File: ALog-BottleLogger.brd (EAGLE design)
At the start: 120.7 x 44.5 mm, 105 parts, among them IC2 ATMEGA644M, J6 5.5x2.1mm Barrel, Q10 MOSFET_PCH-IRLML2244, Q11 220mA/50V/3.5Ω, Q12 4.3A/20V/54mΩ, Q13 MOSFET-NCH-BSS138, Q5 4.3A/20V/54mΩ, Q7 4.3A/20V/54mΩ, Q8 220mA/50V/3.5Ω, Q9 220mA/50V/3.5Ω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

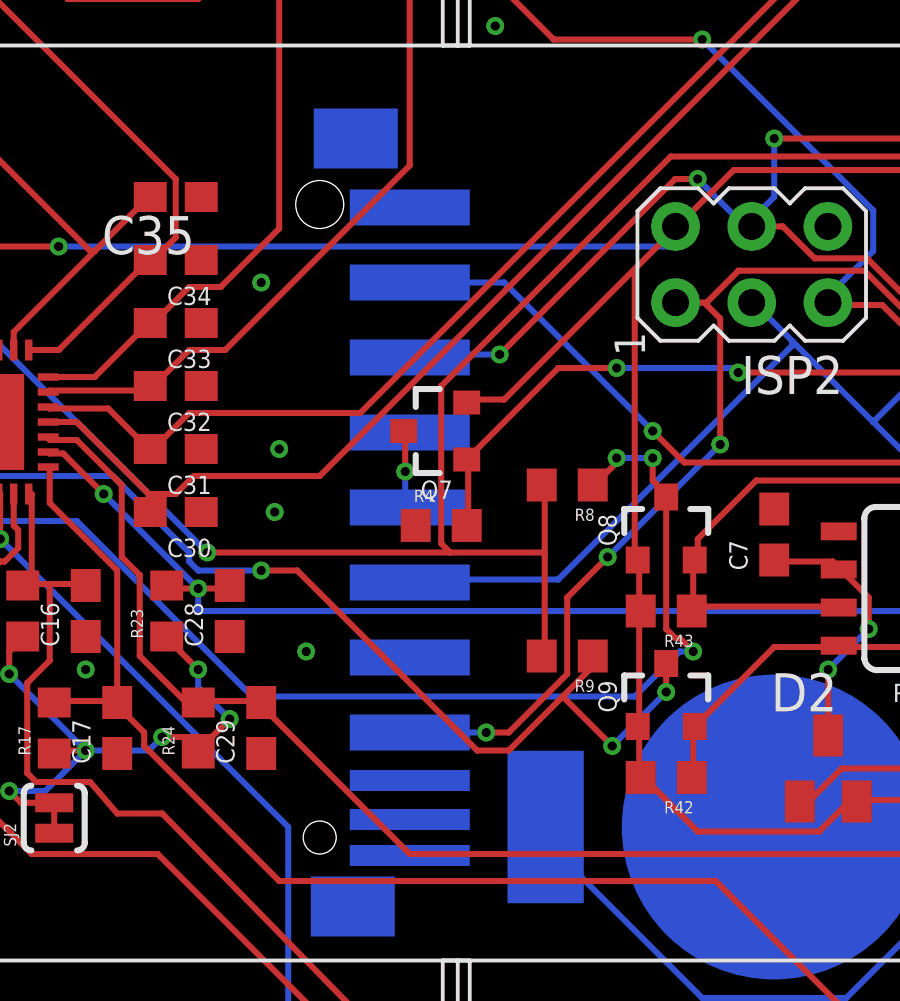
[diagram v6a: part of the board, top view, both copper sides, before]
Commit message: Minor trace fixes, back silkscreen info additions
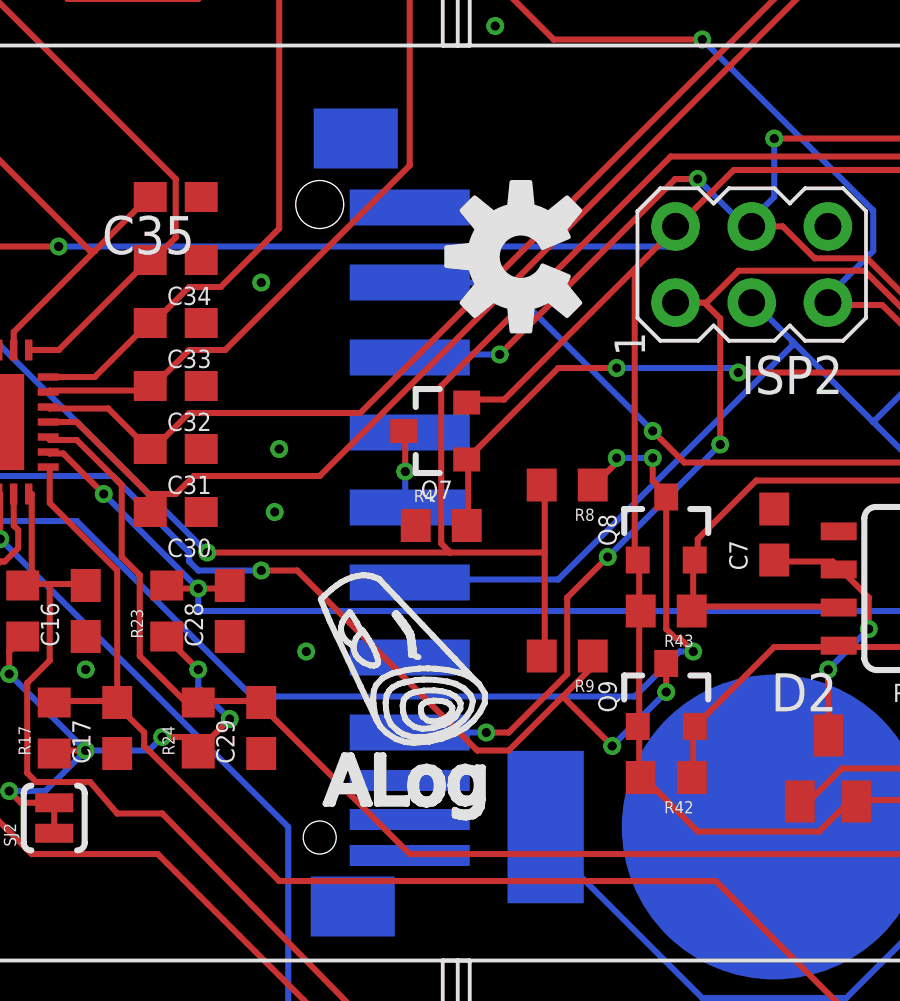
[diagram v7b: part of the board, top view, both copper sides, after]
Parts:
- added LOGO2: OSHW-LOGOM, SparkFun-Aesthetics:OSHW-LOGO-M
- added U$13: (no value), csandell:MN_SILK
- added U$14: ALOG_LOGO_V1_5.5MM, awickert:ALOG_LOGO_V1_SMALL
- added U$15: NWLOGO_MED, awickert:NWLOGO_MED
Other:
- board text added: "ALog BottleLogger v3.0.0 ---------------------------------- Open-source scientific data logger ---------------------------------- Made in Minnesota"
- board text added: "Developed in part at the University of Minnesota in parntnership with Northern Widget LLC"
- board text added: "Open-source for the outdoors"
- board text added: "TM"
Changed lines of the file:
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@@
 <?xml version="1.0" encoding="utf-8"?>
 <!DOCTYPE eagle SYSTEM "eagle.dtd">
-<eagle version="8.3.0">
+<eagle version="8.4.0">
 <drawing>
 <settings>
@@
 <text x="110.93775" y="37.02925" size="1.27" layer="51" font="vector" ratio="10" rot="R225">GND</text>
 <text x="107.63775" y="37.02925" size="1.27" layer="51" font="vector" ratio="10" rot="R225">BATT</text>
+<text x="86.4" y="22.8" size="1.4224" layer="22" ratio="20" rot="MR0" align="bottom-right">ALog BottleLogger v3.0.0
+----------------------------------
+Open-source scientific
+data logger
+----------------------------------
+Made in Minnesota</text>
+<text x="76.2" y="18.3" size="1.778" layer="22" ratio="20" rot="MR0" align="bottom-right">Open-source for the outdoors</text>
+<text x="75" y="19.8" size="0.6096" layer="22" ratio="20" rot="MR0" align="bottom-right">TM</text>
+<text x="106.35" y="15" size="1.4224" layer="22" ratio="20" rot="MR0" align="top-left">Developed in part at the
+University of Minnesota in
+parntnership with
+Northern Widget LLC</text>
+<text x="73.7444" y="12.978" size="0.6096" layer="22" rot="MR0">TM</text>
 </plain>
 <attributes>
@@
 <param name="dpMaxLengthDifference" value="10mm"/>
 <param name="dpGapFactor" value="2.5"/>
-<param name="checkGrid" value="0"/>
-<param name="checkAngle" value="0"/>
 <param name="checkFont" value="1"/>
 <param name="checkRestrict" value="1"/>
+<param name="checkStop" value="0"/>
 <param name="useDiameter" value="13"/>
 <param name="maxErrors" value="50"/>
@@
 </element>
 <element name="C7" library="rcl" package="C0603" value="0.1uF" x="53.25" y="21.15" rot="R90"/>
+<element name="U$13" library="csandell" package="MN_SILK" value="" x="77.25" y="23.25"/>
+<element name="LOGO2" library="SparkFun-Aesthetics" package="OSHW-LOGO-M" value="OSHW-LOGOM" x="44.8066" y="30.4108" smashed="yes" rot="R90"/>
+<element name="U$14" library="awickert" package="ALOG_LOGO_V1_SMALL" value="ALOG_LOGO_V1_5.5MM" x="40.9642" y="16.9232" smashed="yes"/>
+<element name="U$15" library="awickert" package="NWLOGO_MED" value="NWLOGO_MED" x="77.9234" y="11.1888" smashed="yes" rot="MR0"/>
 </elements>
 <signals>
@@
 </board>
 </drawing>
+<compatibility>
+<note version="6.3" minversion="6.2.2" severity="warning">
+Since Version 6.2.2 text objects can contain more than one line,
+which will not be processed correctly with this version.
+</note>
+</compatibility>
 </eagle>

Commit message: ordered for AGU meeting
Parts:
- moved U$15 10.4 mm to (67.6, 11.5)
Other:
- board text added: "ALog BottleLogger v3.0.0 ---------------------- Open-source scientific data logger ---------------------- Made in Minnesota"
- board text removed: "ALog BottleLogger v3.0.0 ---------------------------------- Open-source scientific data logger ---------------------------------- Made in Minnesota"
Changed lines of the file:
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@@
 <?xml version="1.0" encoding="utf-8"?>
 <!DOCTYPE eagle SYSTEM "eagle.dtd">
-<eagle version="8.4.0">
+<eagle version="8.3.1">
 <drawing>
 <settings>
@@
 <text x="107.63775" y="37.02925" size="1.27" layer="51" font="vector" ratio="10" rot="R225">BATT</text>
 <text x="86.4" y="22.8" size="1.4224" layer="22" ratio="20" rot="MR0" align="bottom-right">ALog BottleLogger v3.0.0
-----------------------------------
+----------------------
 Open-source scientific
 data logger
-----------------------------------
+----------------------
 Made in Minnesota</text>
-<text x="76.2" y="18.3" size="1.778" layer="22" ratio="20" rot="MR0" align="bottom-right">Open-source for the outdoors</text>
-<text x="75" y="19.8" size="0.6096" layer="22" ratio="20" rot="MR0" align="bottom-right">TM</text>
+<text x="74.25" y="17.7" size="1.778" layer="22" ratio="20" rot="MR0" align="bottom-right">Open-source for the outdoors</text>
+<text x="73.05" y="19.2" size="0.6096" layer="22" ratio="20" rot="MR0" align="bottom-right">TM</text>
 <text x="106.35" y="15" size="1.4224" layer="22" ratio="20" rot="MR0" align="top-left">Developed in part at the
 University of Minnesota in
 parntnership with
 Northern Widget LLC</text>
-<text x="73.7444" y="12.978" size="0.6096" layer="22" rot="MR0">TM</text>
+<text x="63.0944" y="15.378" size="0.6096" layer="22" rot="MR0">TM</text>
 </plain>
 <attributes>
@@
 <param name="dpMaxLengthDifference" value="10mm"/>
 <param name="dpGapFactor" value="2.5"/>
+<param name="checkGrid" value="0"/>
+<param name="checkAngle" value="0"/>
 <param name="checkFont" value="1"/>
 <param name="checkRestrict" value="1"/>
-<param name="checkStop" value="0"/>
 <param name="useDiameter" value="13"/>
 <param name="maxErrors" value="50"/>
@@
 <element name="LOGO2" library="SparkFun-Aesthetics" package="OSHW-LOGO-M" value="OSHW-LOGOM" x="44.8066" y="30.4108" smashed="yes" rot="R90"/>
 <element name="U$14" library="awickert" package="ALOG_LOGO_V1_SMALL" value="ALOG_LOGO_V1_5.5MM" x="40.9642" y="16.9232" smashed="yes"/>
-<element name="U$15" library="awickert" package="NWLOGO_MED" value="NWLOGO_MED" x="77.9234" y="11.1888" smashed="yes" rot="MR0"/>
+<element name="U$15" library="awickert" package="NWLOGO_MED" value="NWLOGO_MED" x="67.5734" y="11.4888" smashed="yes" rot="MR0"/>
 </elements>
 <signals>
